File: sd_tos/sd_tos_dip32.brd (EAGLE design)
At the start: 19.5 x 63.5 mm, 20 parts, among them IC1 MEGA16-A, IC3 74HCT595D

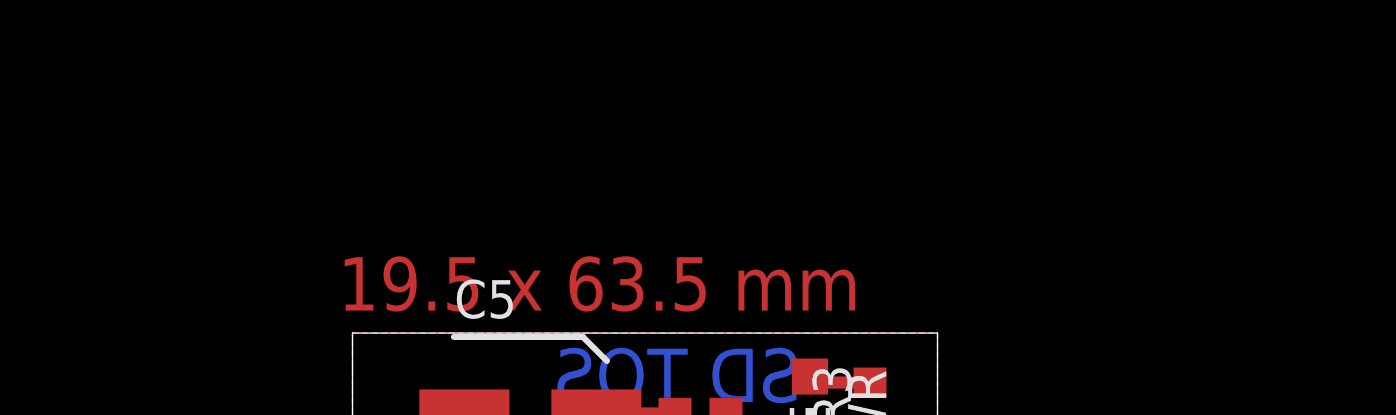
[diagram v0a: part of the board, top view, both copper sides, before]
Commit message: added version for 28 pin EPROMs (e.g. STFM)
git-svn-id: https://subversion.assembla.com/svn/atarijookie/trunk@939 0d2ca917-fb58-4453-bb26-a698c01b0940
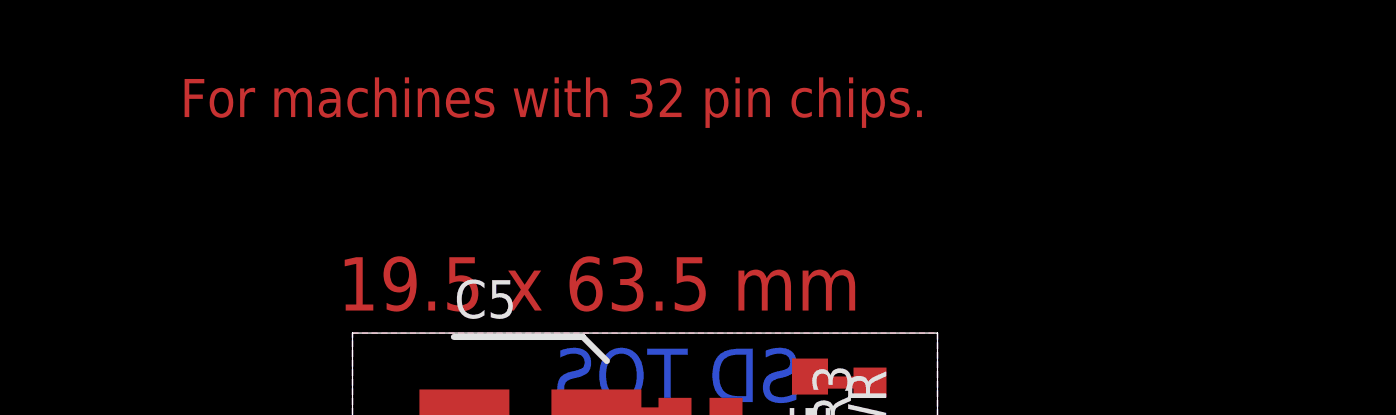
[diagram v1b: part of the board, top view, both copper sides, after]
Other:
- board text added: "For machines with 32 pin chips."
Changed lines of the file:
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@@
 <grid distance="0.1" unitdist="mm" unit="mm" style="lines" multiple="1" display="yes" altdistance="0.01" altunitdist="mm" altunit="mm"/>
 <layers>
-<layer number="1" name="Top" color="4" fill="1" visible="no" active="yes"/>
+<layer number="1" name="Top" color="4" fill="1" visible="yes" active="yes"/>
 <layer number="2" name="Route2" color="1" fill="3" visible="no" active="no"/>
 <layer number="3" name="Route3" color="4" fill="3" visible="no" active="no"/>
@@
 <text x="14.75" y="0.5" size="1.778" layer="1" font="vector" ratio="20">x - drill through vias to remove connection</text>
 <text x="21.25" y="-2" size="1.778" layer="1" font="vector" ratio="20">between top and bottom layer</text>
+<text x="29" y="74.7" size="1.27" layer="1" font="vector" ratio="20">For machines with 32 pin chips.</text>
 </plain>
 <attributes>

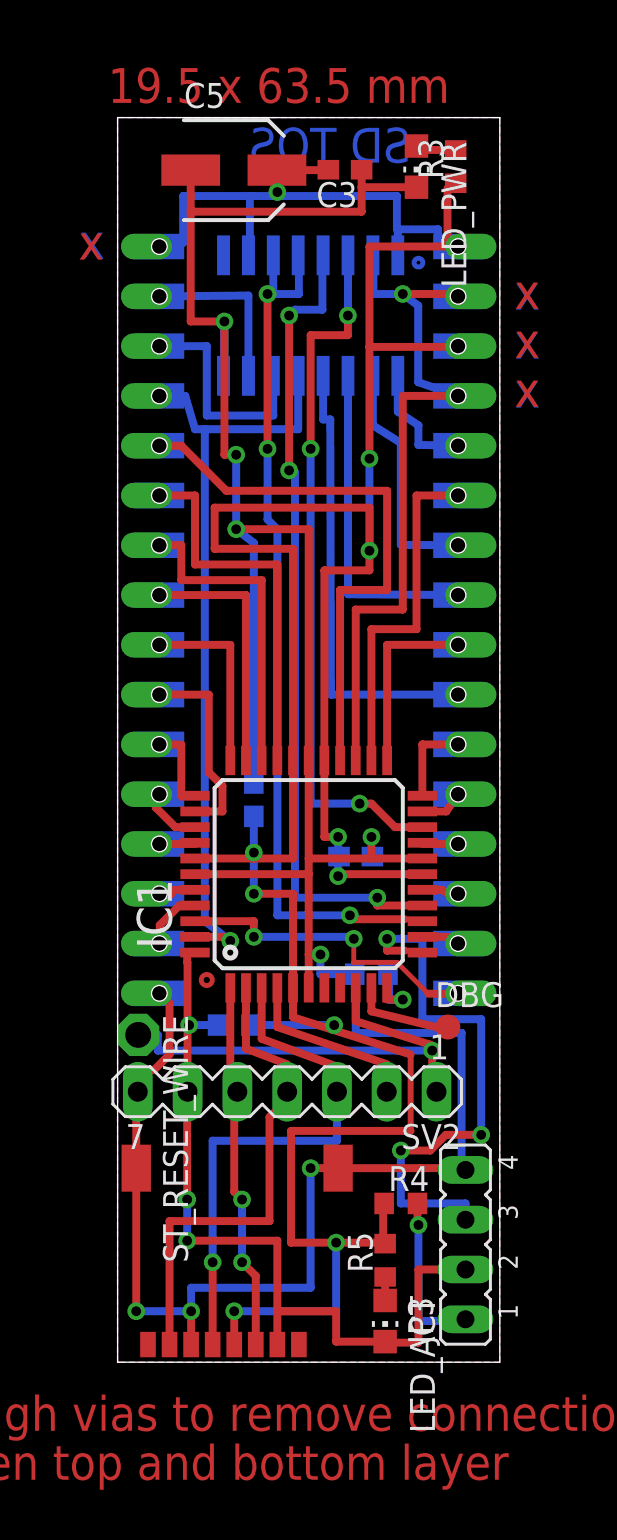
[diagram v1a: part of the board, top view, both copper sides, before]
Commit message: micro sd connector altered to match the real one
git-svn-id: https://subversion.assembla.com/svn/atarijookie/trunk@941 0d2ca917-fb58-4453-bb26-a698c01b0940
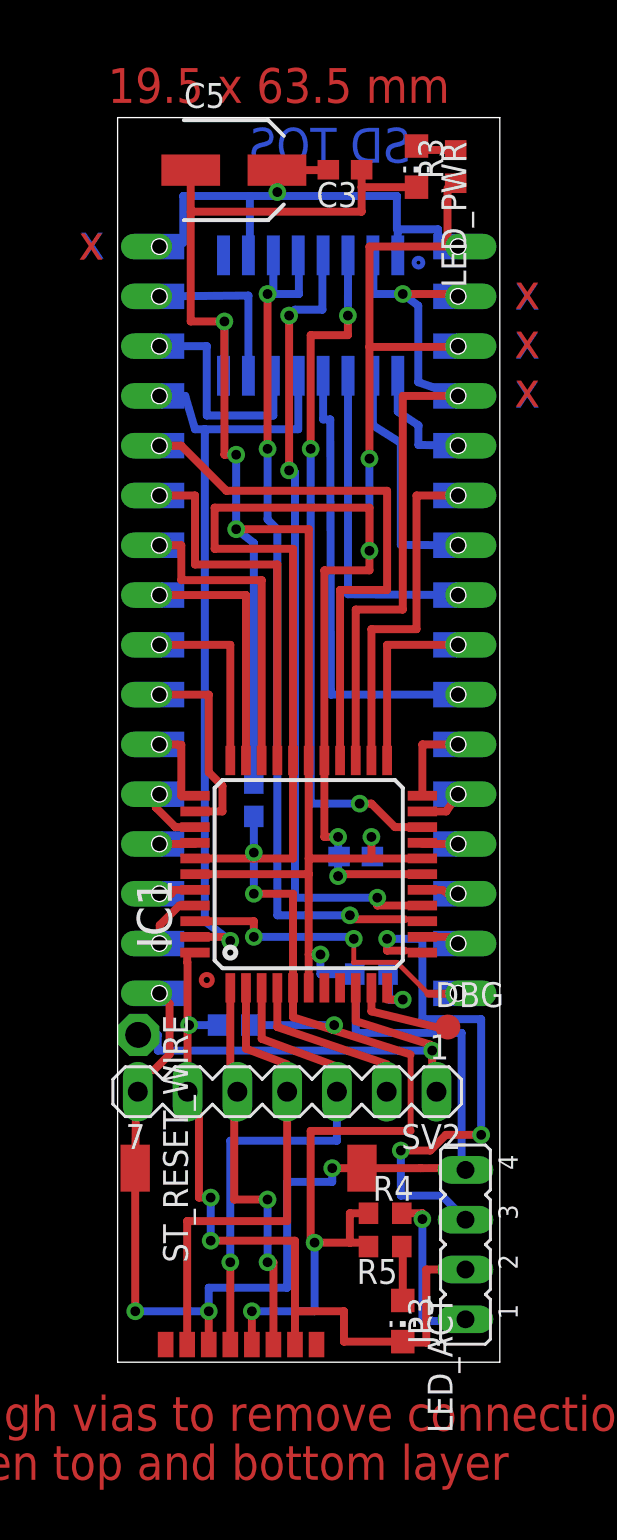
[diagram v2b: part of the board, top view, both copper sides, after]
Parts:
- moved R4 0.94 mm to (48.4, 11.6)
- moved LED_ACT 0.90 mm to (49.3, 6.10)
- moved U$3 0.90 mm to (41.6, 4.90)
- moved R5 0.70 mm to (48.4, 9.90), turned to 180 degrees
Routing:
- net VCC: track 174.9 -> 170.5 mm
- net N$2: track 1.20 -> 2.80 mm
- net MOSI: track 19.0 -> 20.6 mm
- net SCK: track 27.2 -> 26.3 mm
- net BTN: track 29.5 -> 28.8 mm
- net SD_CS: track 41.5 -> 41.0 mm
- removed copper zone on layer 1, net GND
- removed copper zone on layer 16, net GND
